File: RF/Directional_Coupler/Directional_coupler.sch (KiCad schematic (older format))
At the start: 56 parts, among them J1 RF in, J2 RF out, J3 Singal, T1 30T, T2 1T, U1 LMH6609MF, U2 LMV358, U3 AD8307, U4 AD8307, U5 LMH6609MF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

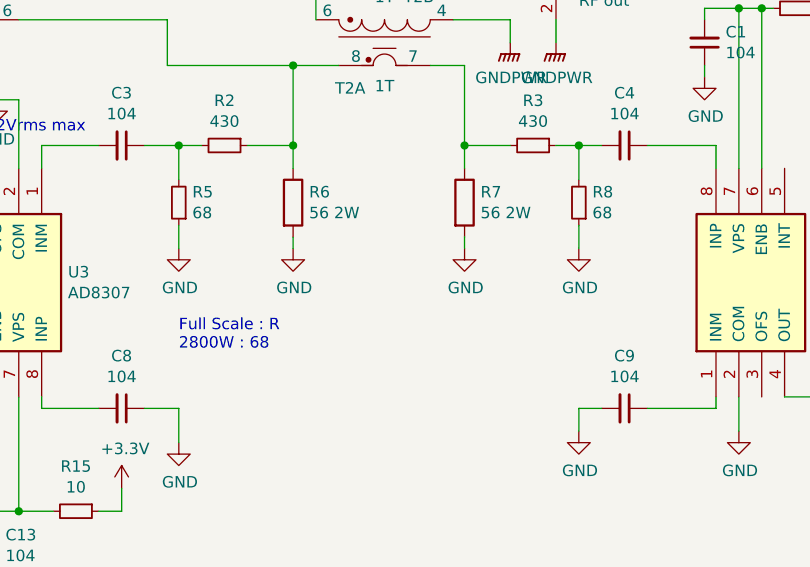
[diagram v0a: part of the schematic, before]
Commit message: Controller Circuit Done. Now routing
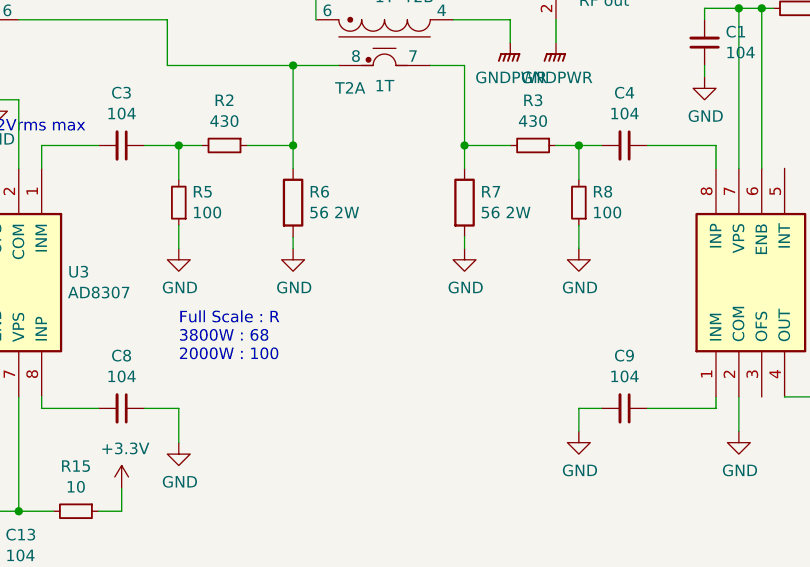
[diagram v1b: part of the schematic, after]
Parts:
- R5, R8: value 68 -> 100
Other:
- note added: "Full Scale : R\n3800W : 68\n2000W : 100"
- note removed: "Full Scale : R\n2800W : 68"
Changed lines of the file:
@@
 P 5100 2950
 F 0 "R5" H 5041 2904 50  0000 R CNN
-F 1 "68" H 5041 2995 50  0000 R CNN
+F 1 "100" H 5041 2995 50  0000 R CNN
 F 2 "Resistors_SMD:R_0805" H 5100 2950 50  0001 C CNN
 F 3 "~" H 5100 2950 50  0001 C CNN
@@
 P 6850 2950
 F 0 "R8" H 6791 2904 50  0000 R CNN
-F 1 "68" H 6791 2995 50  0000 R CNN
+F 1 "100" H 6791 2995 50  0000 R CNN
 F 2 "Resistors_SMD:R_0805" H 6850 2950 50  0001 C CNN
 F 3 "~" H 6850 2950 50  0001 C CNN
@@
 Text Notes 4300 2650 0    50   ~ 0
 2Vrms max
-Text Notes 5100 3600 0    50   ~ 0
-Full Scale : R\n2800W : 68
+Text Notes 5100 3650 0    50   ~ 0
+Full Scale : R\n3800W : 68\n2000W : 100
 $Comp
 L Device:C_Small C4
